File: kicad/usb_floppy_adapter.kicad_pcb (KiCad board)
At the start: 2 copper layers, 48 x 19 mm, 28 parts, among them J1 Conn_02x17_Odd_Even, J2 MICRO_USB_B, J3 Conn_01x02, J4 Conn_01x04, J5 GS2, J6 GS2, J7 GS3, U1 LM1117-3.3, U2 STM32F103C8Tx, U3 USBLC6-2SC6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

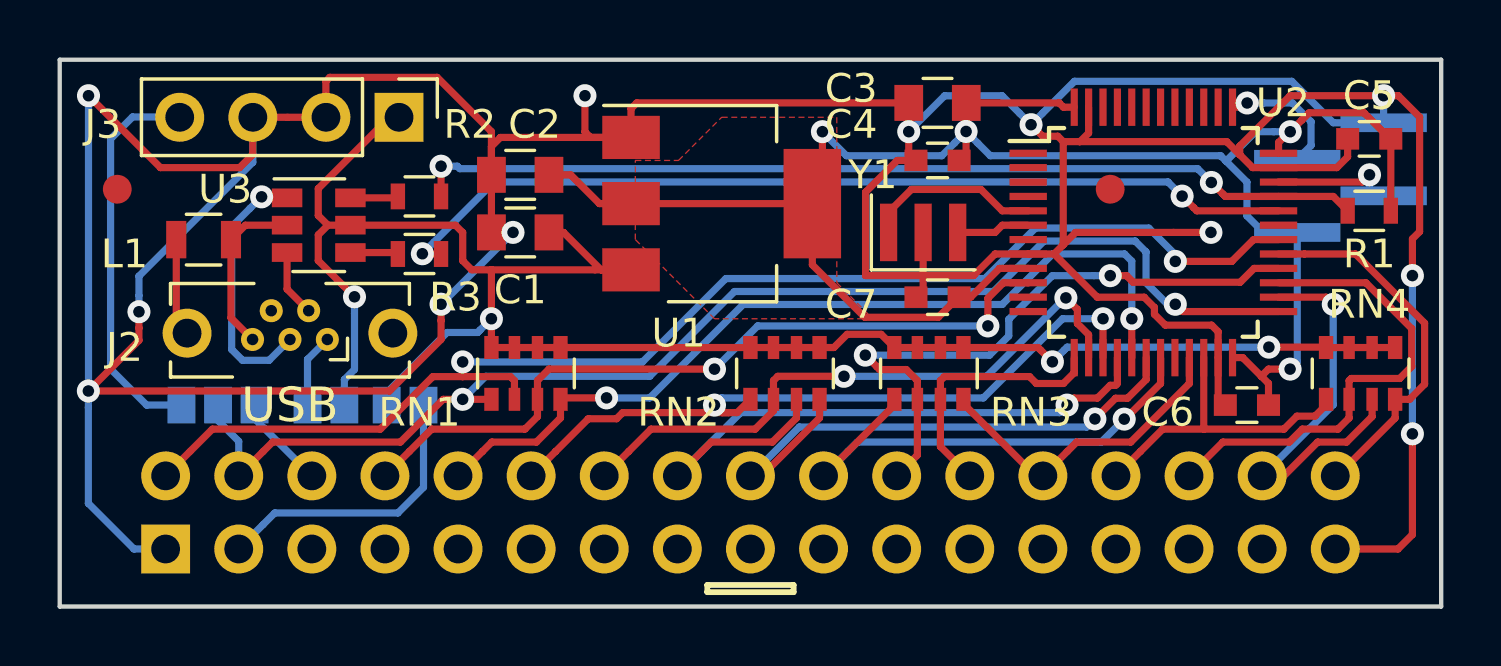
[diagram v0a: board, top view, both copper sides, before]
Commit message: Preparations for first prototype run
- Tie BOOT0 to GND to ensure proper boot-up
- Mark all unused MCU pins in the schematic as N/C
- Double the width of the most important 5V and 12V traces
- Move some traces further away from pads
- Optimize parameters of Copper Fills
- Add meta data and revision number (revision 0)
- Include URL and revision number in silk screen text
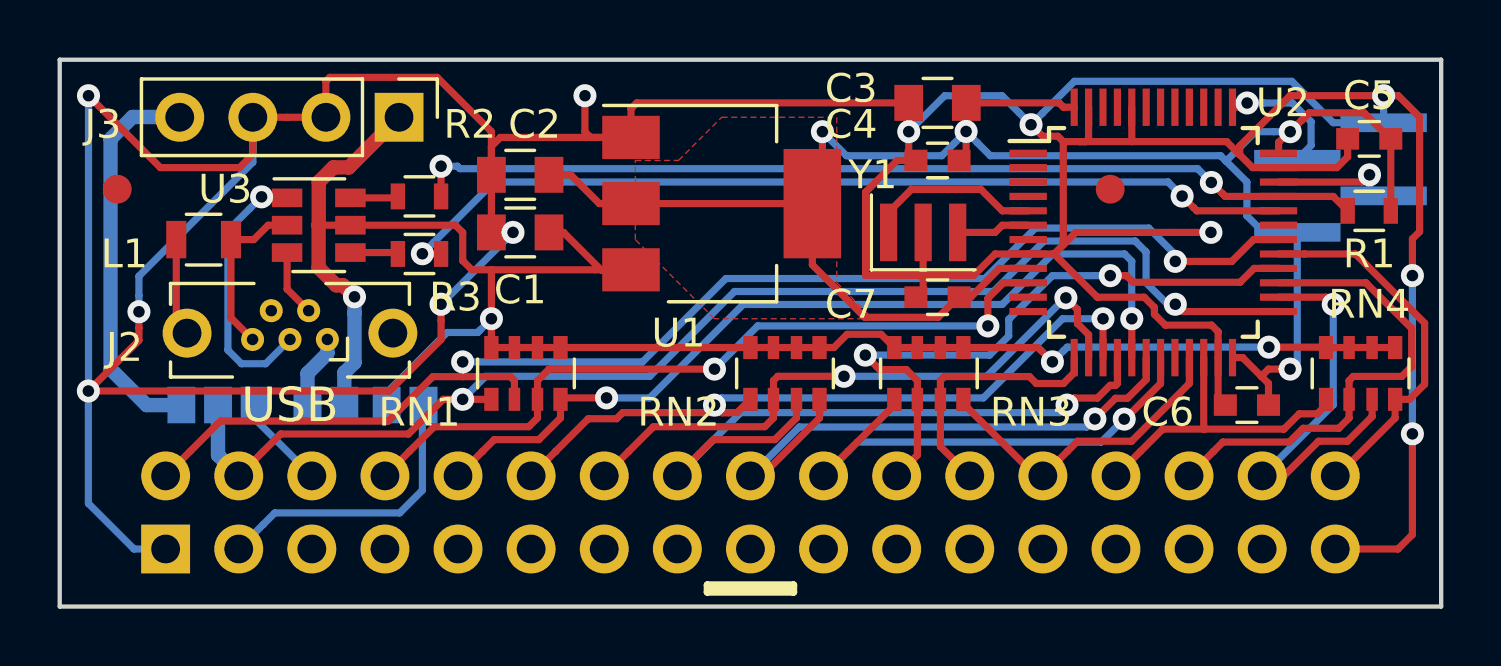
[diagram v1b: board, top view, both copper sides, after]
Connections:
- U2 pad 44: Net-(U2-Pad44) -> GND
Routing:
- net GND: track 189.4 -> 190.7 mm
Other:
- board text added: "Design by usermo.de, v.0"
- board text removed: "Design © 2018 B.Freisen"
